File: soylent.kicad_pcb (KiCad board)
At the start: 2 copper layers, 34.5 x 43.2 mm, 23 parts, among them J1 DB9_Female, J2 Conn_01x04, J3 Conn_01x04, J4 Conn_02x03_Counter_Clockwise, Q1 BC847BPN, Q2 BC847BPN, U1 ATtiny202-SS, U2 MIC5504-3.3YM5

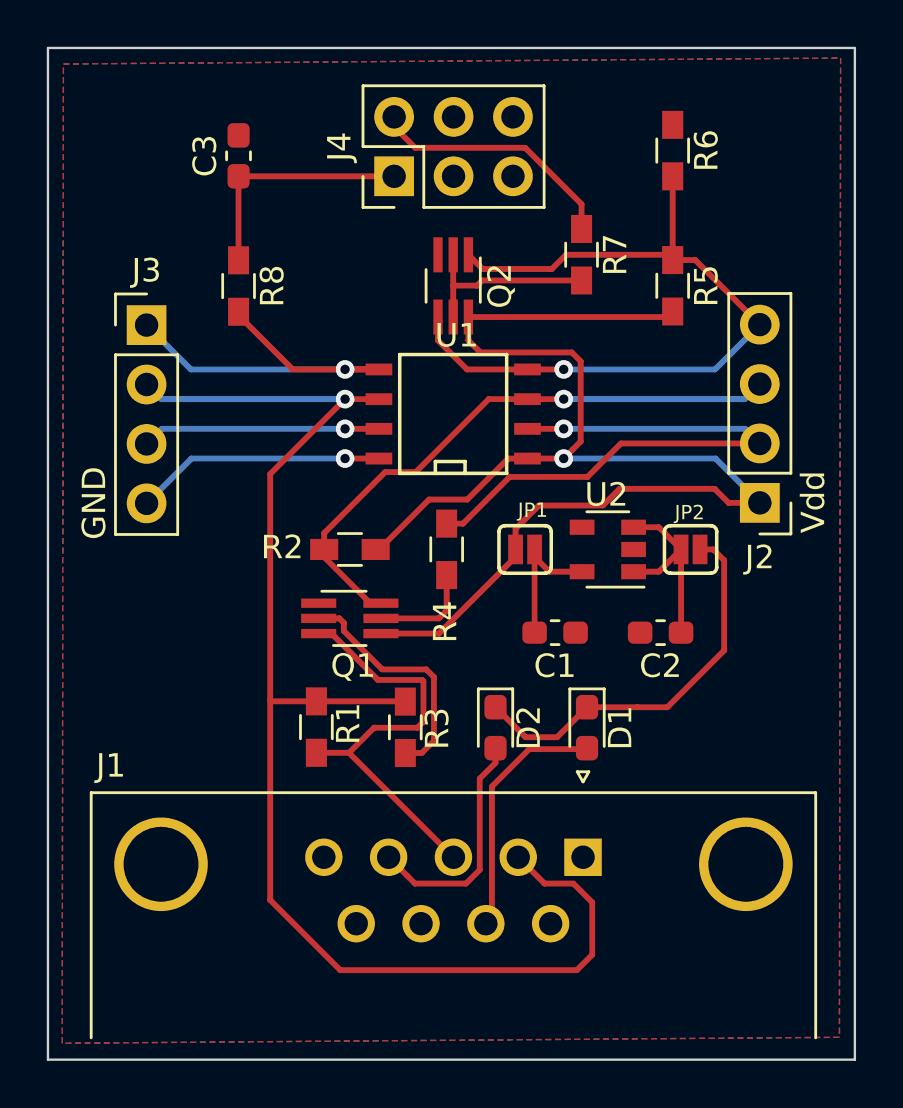
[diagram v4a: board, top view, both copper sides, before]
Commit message: Add a jumper for UPDI inhibit
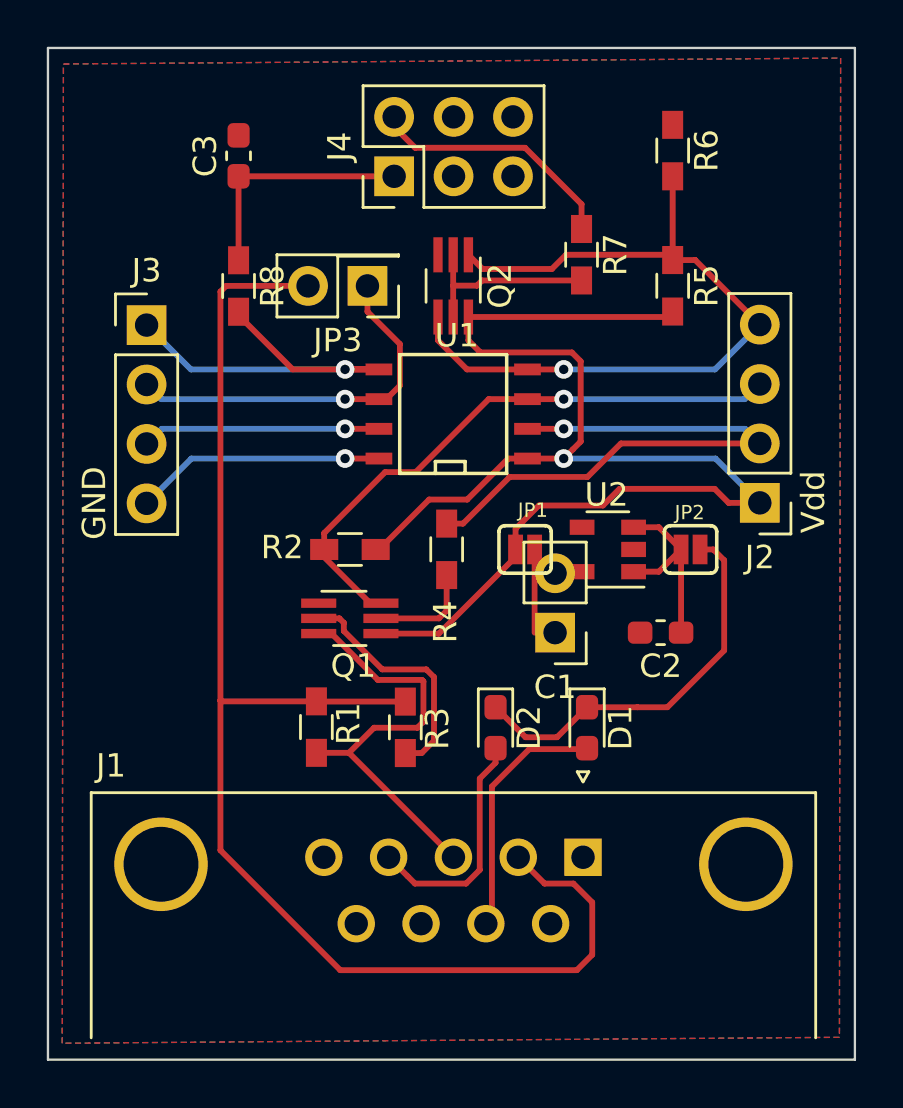
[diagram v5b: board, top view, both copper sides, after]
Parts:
- added JP3: Jumper_2_Bridged, Connector_PinHeader_2.54mm:PinHeader_2x01_P2.54mm_Vertical, F.Cu at (235.6, 29.9)
- C1: footprint Capacitor_SMD:C_0603_1608Metric_Pad1.05x0.95mm_HandSolder -> Connector_PinHeader_2.54mm:PinHeader_1x02_P2.54mm_Vertical
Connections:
- J3 pad 2: /TD -> /UPDI
- U1 pad 6: /TD -> /UPDI
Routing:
- net /UPDI: track 0.00 -> 16.2 mm, vias 0 -> 1
- net /TD: track 60.6 -> 60.5 mm, vias 1 -> 0

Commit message: Add a transistor to simulate mic
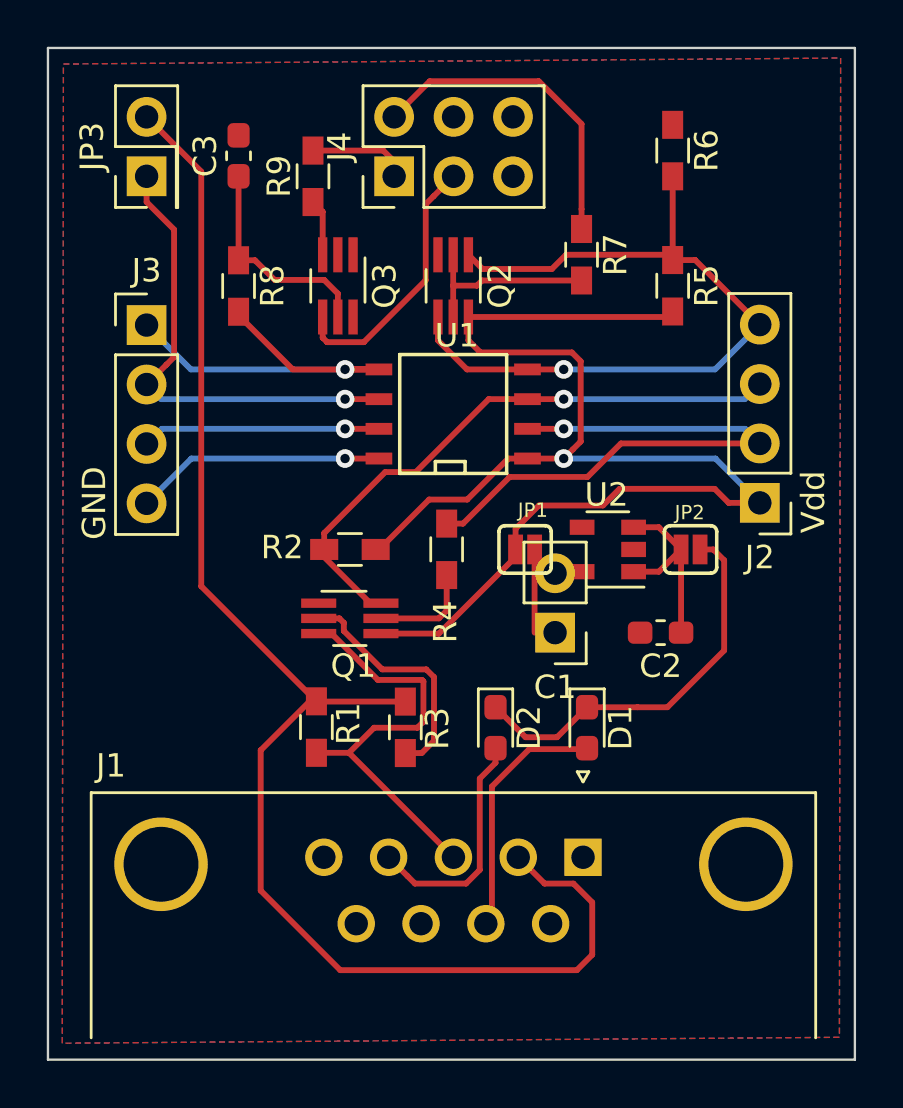
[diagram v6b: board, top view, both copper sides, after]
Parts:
- added Q3: BC847BPN, TO_SOT_Packages_SMD:SOT-363_SC-70-6_Handsoldering, F.Cu at (234.3, 29.9)
- added R9: 100R, Resistors_SMD:R_0603_HandSoldering, F.Cu at (233.2, 25.2)
- moved JP3 10.5 mm to (226.1, 25.2), turned to 90 degrees
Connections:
- J4 pad 1: Net-(C3-Pad1) -> Net-(J4-Pad1)
- J4 pad 3: (no net) -> Net-(J4-Pad3)
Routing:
- net Net-(J4-Pad3): track 0.00 -> 11.4 mm
- net Net-(J4-Pad1): track 0.00 -> 4.11 mm
- net /UPDI: track 16.2 -> 20.1 mm
- net Net-(J4-Pad2): track 10.9 -> 13.9 mm
- net /TD: track 60.5 -> 63.4 mm
- net Net-(Q3-Pad3): track 0.00 -> 2.43 mm
- net Net-(C3-Pad1): track 10.2 -> 9.43 mm

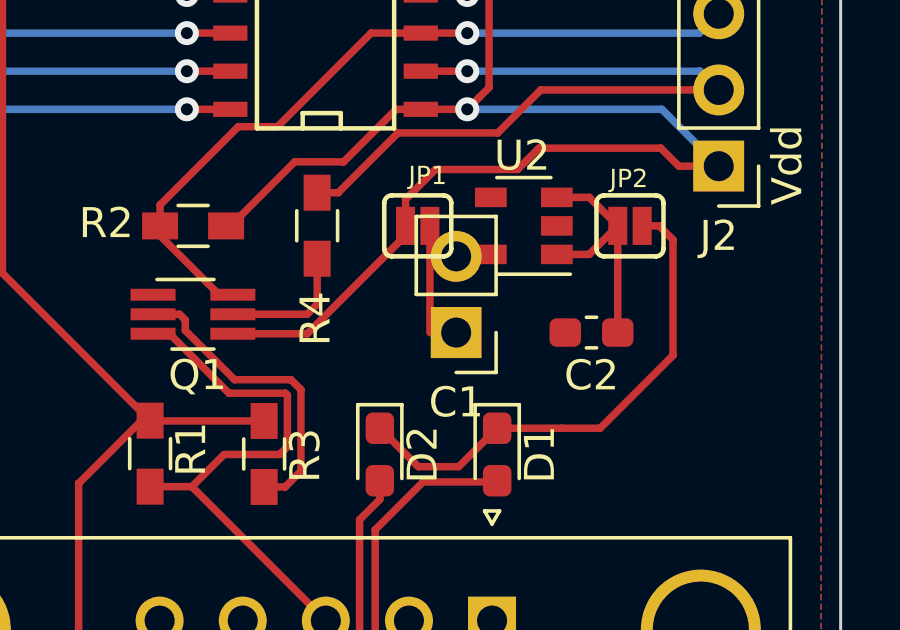
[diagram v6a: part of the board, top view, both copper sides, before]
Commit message: Correct bad footprint
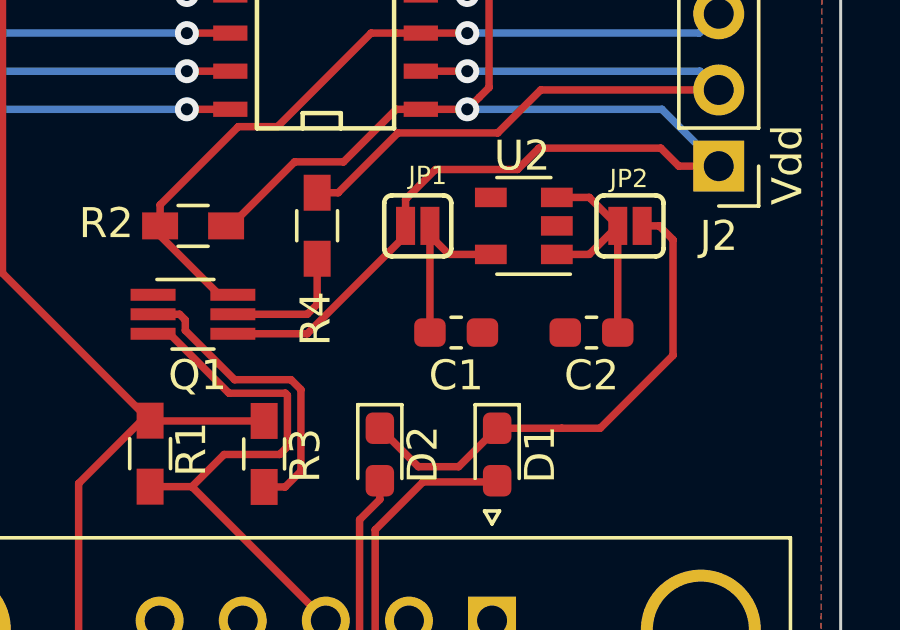
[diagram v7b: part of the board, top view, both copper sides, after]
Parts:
- C1: footprint Connector_PinHeader_2.54mm:PinHeader_1x02_P2.54mm_Vertical -> Capacitor_SMD:C_0603_1608Metric_Pad1.05x0.95mm_HandSolder
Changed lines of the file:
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@@
     (add_net "Net-(C3-Pad1)")
     (add_net "Net-(D1-Pad1)")
-    (add_net "Net-(J1-Pad1)")
-    (add_net "Net-(J1-Pad6)")
-    (add_net "Net-(J1-Pad8)")
-    (add_net "Net-(J1-Pad9)")
     (add_net "Net-(J4-Pad1)")
     (add_net "Net-(J4-Pad2)")
     (add_net "Net-(J4-Pad3)")
-    (add_net "Net-(J4-Pad4)")
-    (add_net "Net-(J4-Pad5)")
     (add_net "Net-(Q1-Pad2)")
     (add_net "Net-(Q1-Pad5)")
     (add_net "Net-(Q2-Pad2)")
     (add_net "Net-(Q3-Pad3)")
-    (add_net "Net-(U2-Pad4)")
     (add_net VDD)
+  )
+  (module Capacitor_SMD:C_0603_1608Metric_Pad1.05x0.95mm_HandSolder (layer F.Cu)
+    (at 243.572 44.7548 180)
+    (descr "Capacitor SMD 0603 (1608 Metric), square (rectangular) end terminal, IPC_7351 nominal with elongated pad for handsoldering. (Body size source: http://www.tortai-tech.com/upload/download/2011102023233369053.pdf), generated with kicad-footprint-generator")
+    (tags "capacitor handsolder")
+    (attr smd)
+    (fp_text reference C1 (at 0 -1.43) (layer F.SilkS)
+      (effects (font (size 1 1) (thickness 0.15)))
+    )
+    (fp_text value 1u (at 0 1.43) (layer F.Fab)
+      (effects (font (size 1 1) (thickness 0.15)))
+    )
+    (fp_text user %R (at 0 0) (layer F.Fab)
+      (effects (font (size 0.4 0.4) (thickness 0.06)))
+    )
+    (fp_line (start 1.65 0.73) (end -1.65 0.73) (layer F.CrtYd) (width 0.05))
+    (fp_line (start 1.65 -0.73) (end 1.65 0.73) (layer F.CrtYd) (width 0.05))
+    (fp_line (start -1.65 -0.73) (end 1.65 -0.73) (layer F.CrtYd) (width 0.05))
+    (fp_line (start -1.65 0.73) (end -1.65 -0.73) (layer F.CrtYd) (width 0.05))
+    (fp_line (start -0.171267 0.51) (end 0.171267 0.51) (layer F.SilkS) (width 0.12))
+    (fp_line (start -0.171267 -0.51) (end 0.171267 -0.51) (layer F.SilkS) (width 0.12))
+    (fp_line (start 0.8 0.4) (end -0.8 0.4) (layer F.Fab) (width 0.1))
+    (fp_line (start 0.8 -0.4) (end 0.8 0.4) (layer F.Fab) (width 0.1))
+    (fp_line (start -0.8 -0.4) (end 0.8 -0.4) (layer F.Fab) (width 0.1))
+    (fp_line (start -0.8 0.4) (end -0.8 -0.4) (layer F.Fab) (width 0.1))
+    (pad 2 smd roundrect (at 0.875 0 180) (size 1.05 0.95) (layers F.Cu F.Paste F.Mask) (roundrect_rratio 0.25)
+      (net 7 "Net-(C1-Pad2)"))
+    (pad 1 smd roundrect (at -0.875 0 180) (size 1.05 0.95) (layers F.Cu F.Paste F.Mask) (roundrect_rratio 0.25)
+      (net 1 GND))
+    (model ${KISYS3DMOD}/Capacitor_SMD.3dshapes/C_0603_1608Metric.wrl
+      (at (xyz 0 0 0))
+      (scale (xyz 1 1 1))
+      (rotate (xyz 0 0 0))
+    )
   )
   (module Resistors_SMD:R_0603_HandSoldering (layer F.Cu)
@@
       (net 20 /UPDI))
     (model ${KISYS3DMOD}/Connector_PinHeader_2.54mm.3dshapes/PinHeader_2x01_P2.54mm_Vertical.wrl
-      (at (xyz 0 0 0))
-      (scale (xyz 1 1 1))
-      (rotate (xyz 0 0 0))
-    )
-  )
-  (module Connector_PinHeader_2.54mm:PinHeader_1x02_P2.54mm_Vertical (layer F.Cu)
-    (at 243.572 44.7548 180)
-    (descr "Through hole straight pin header, 1x02, 2.54mm pitch, single row")
-    (tags "Through hole pin header THT 1x02 2.54mm single row")
-    (fp_text reference C1 (at 0 -2.33) (layer F.SilkS)
-      (effects (font (size 1 1) (thickness 0.15)))
-    )
-    (fp_text value 1u (at 0 4.87) (layer F.Fab)
-      (effects (font (size 1 1) (thickness 0.15)))
-    )
-    (fp_text user %R (at 0 1.27 90) (layer F.Fab)
-      (effects (font (size 1 1) (thickness 0.15)))
-    )
-    (fp_line (start 1.8 -1.8) (end -1.8 -1.8) (layer F.CrtYd) (width 0.05))
-    (fp_line (start 1.8 4.35) (end 1.8 -1.8) (layer F.CrtYd) (width 0.05))
-    (fp_line (start -1.8 4.35) (end 1.8 4.35) (layer F.CrtYd) (width 0.05))
-    (fp_line (start -1.8 -1.8) (end -1.8 4.35) (layer F.CrtYd) (width 0.05))
-    (fp_line (start -1.33 -1.33) (end 0 -1.33) (layer F.SilkS) (width 0.12))
-    (fp_line (start -1.33 0) (end -1.33 -1.33) (layer F.SilkS) (width 0.12))
-    (fp_line (start -1.33 1.27) (end 1.33 1.27) (layer F.SilkS) (width 0.12))
-    (fp_line (start 1.33 1.27) (end 1.33 3.87) (layer F.SilkS) (width 0.12))
-    (fp_line (start -1.33 1.27) (end -1.33 3.87) (layer F.SilkS) (width 0.12))
-    (fp_line (start -1.33 3.87) (end 1.33 3.87) (layer F.SilkS) (width 0.12))
-    (fp_line (start -1.27 -0.635) (end -0.635 -1.27) (layer F.Fab) (width 0.1))
-    (fp_line (start -1.27 3.81) (end -1.27 -0.635) (layer F.Fab) (width 0.1))
-    (fp_line (start 1.27 3.81) (end -1.27 3.81) (layer F.Fab) (width 0.1))
-    (fp_line (start 1.27 -1.27) (end 1.27 3.81) (layer F.Fab) (width 0.1))
-    (fp_line (start -0.635 -1.27) (end 1.27 -1.27) (layer F.Fab) (width 0.1))
-    (pad 2 thru_hole oval (at 0 2.54 180) (size 1.7 1.7) (drill 1) (layers *.Cu *.Mask)
-      (net 7 "Net-(C1-Pad2)"))
-    (pad 1 thru_hole rect (at 0 0 180) (size 1.7 1.7) (drill 1) (layers *.Cu *.Mask)
-      (net 1 GND))
-    (model ${KISYS3DMOD}/Connector_PinHeader_2.54mm.3dshapes/PinHeader_1x02_P2.54mm_Vertical.wrl
       (at (xyz 0 0 0))
       (scale (xyz 1 1 1))
@@
   (segment (start 248.3642 31.2626) (end 248.5992 31.0276) (width 0.25) (layer F.Cu) (net 3))
   (segment (start 239.8672 31.2626) (end 248.3642 31.2626) (width 0.25) (layer F.Cu) (net 3))
-  (segment (start 241.8842 41.5163) (end 241.8842 41.1988) (width 0.25) (layer F.Cu) (net 3))
-  (segment (start 238.6053 44.7952) (end 241.8842 41.5163) (width 0.25) (layer F.Cu) (net 3))
-  (segment (start 236.1276 44.7952) (end 238.6053 44.7952) (width 0.25) (layer F.Cu) (net 3))
   (segment (start 241.5707 37.3126) (end 242.3922 37.3126) (width 0.25) (layer F.Cu) (net 3))
   (segment (start 239.8181 39.0652) (end 241.5707 37.3126) (width 0.25) (layer F.Cu) (net 3))
@@
   (segment (start 239.8672 31.2626) (end 239.8672 32.2626) (width 0.25) (layer F.Cu) (net 3))
   (segment (start 245.618 39.3192) (end 246.3292 38.608) (width 0.25) (layer F.Cu) (net 3))
-  (segment (start 241.8842 41.1988) (end 241.8842 40.3138) (width 0.25) (layer F.Cu) (net 3))
   (segment (start 241.8842 40.3138) (end 242.8788 39.3192) (width 0.25) (layer F.Cu) (net 3))
   (segment (start 246.3292 38.608) (end 250.3932 38.608) (width 0.25) (layer F.Cu) (net 3))
@@
   (segment (start 250.9928 39.2076) (end 252.3236 39.2076) (width 0.25) (layer F.Cu) (net 3))
   (segment (start 250.3932 38.608) (end 250.9928 39.2076) (width 0.25) (layer F.Cu) (net 3))
+  (segment (start 241.8842 41.5163) (end 241.8842 41.1988) (width 0.25) (layer F.Cu) (net 3))
+  (segment (start 238.6053 44.7952) (end 241.8842 41.5163) (width 0.25) (layer F.Cu) (net 3))
+  (segment (start 236.1276 44.7952) (end 238.6053 44.7952) (width 0.25) (layer F.Cu) (net 3))
+  (segment (start 241.8842 40.3138) (end 241.8842 41.1988) (width 0.25) (layer F.Cu) (net 3))
   (segment (start 237.945734 48.561301) (end 237.688235 48.8188) (width 0.25) (layer F.Cu) (net 4))
   (segment (start 237.945734 46.841299) (end 237.945734 48.561301) (width 0.25) (layer F.Cu) (net 4))
@@
   (segment (start 243.3295 42.1488) (end 242.697 41.5163) (width 0.25) (layer F.Cu) (net 7))
   (segment (start 244.7275 42.1488) (end 243.3295 42.1488) (width 0.25) (layer F.Cu) (net 7))
-  (segment (start 242.697 41.1988) (end 242.697 44.7548) (width 0.25) (layer F.Cu) (net 7))
+  (segment (start 242.697 44.7548) (end 242.697 41.1988) (width 0.25) (layer F.Cu) (net 7))
   (segment (start 248.008 40.2488) (end 246.9275 40.2488) (width 0.25) (layer F.Cu) (net 8))
   (segment (start 248.958 41.1988) (end 248.008 40.2488) (width 0.25) (layer F.Cu) (net 8))
@@
     (connect_pads (clearance 0.254))
     (min_thickness 0.254)
-    (fill yes (arc_segments 32) (thermal_gap 0.508) (thermal_bridge_width 0.508))
+    (fill (arc_segments 32) (thermal_gap 0.508) (thermal_bridge_width 0.508))
     (polygon
       (pts
@@
     (connect_pads (clearance 0.254))
     (min_thickness 0.254)
-    (fill yes (arc_segments 32) (thermal_gap 0.508) (thermal_bridge_width 0.508))
+    (fill (arc_segments 32) (thermal_gap 0.508) (thermal_bridge_width 0.508))
     (polygon
       (pts

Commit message: Un-tweak routing
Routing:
- net Net-(J4-Pad2): track 13.9 -> 13.1 mm
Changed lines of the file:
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@@
   (segment (start 242.4684 49.7332) (end 244.8986 49.7332) (width 0.25) (layer F.Cu) (net 10))
   (segment (start 240.6122 57.196) (end 240.872199 56.936001) (width 0.25) (layer F.Cu) (net 10))
+  (segment (start 242.336201 21.532599) (end 244.7036 23.899998) (width 0.25) (layer F.Cu) (net 11))
+  (segment (start 244.7036 23.899998) (end 244.7036 26.6504) (width 0.25) (layer F.Cu) (net 11))
+  (segment (start 237.867201 21.532599) (end 242.336201 21.532599) (width 0.25) (layer F.Cu) (net 11))
   (segment (start 244.7036 26.6504) (end 244.7036 27.5004) (width 0.25) (layer F.Cu) (net 11))
-  (segment (start 242.8748 21.1836) (end 244.7036 23.0124) (width 0.25) (layer F.Cu) (net 11))
-  (segment (start 238.2162 21.1836) (end 242.8748 21.1836) (width 0.25) (layer F.Cu) (net 11))
-  (segment (start 244.7036 23.0124) (end 244.7036 26.6504) (width 0.25) (layer F.Cu) (net 11))
-  (segment (start 236.6922 22.7076) (end 238.2162 21.1836) (width 0.25) (layer F.Cu) (net 11))
+  (segment (start 236.6922 22.7076) (end 237.867201 21.532599) (width 0.25) (layer F.Cu) (net 11))
   (segment (start 244.938 47.9438) (end 247.08951 47.9438) (width 0.25) (layer F.Cu) (net 12))
   (segment (start 241.026866 47.9438) (end 242.308266 49.2252) (width 0.25) (layer F.Cu) (net 12))
